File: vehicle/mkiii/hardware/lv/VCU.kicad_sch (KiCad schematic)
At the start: 0 parts

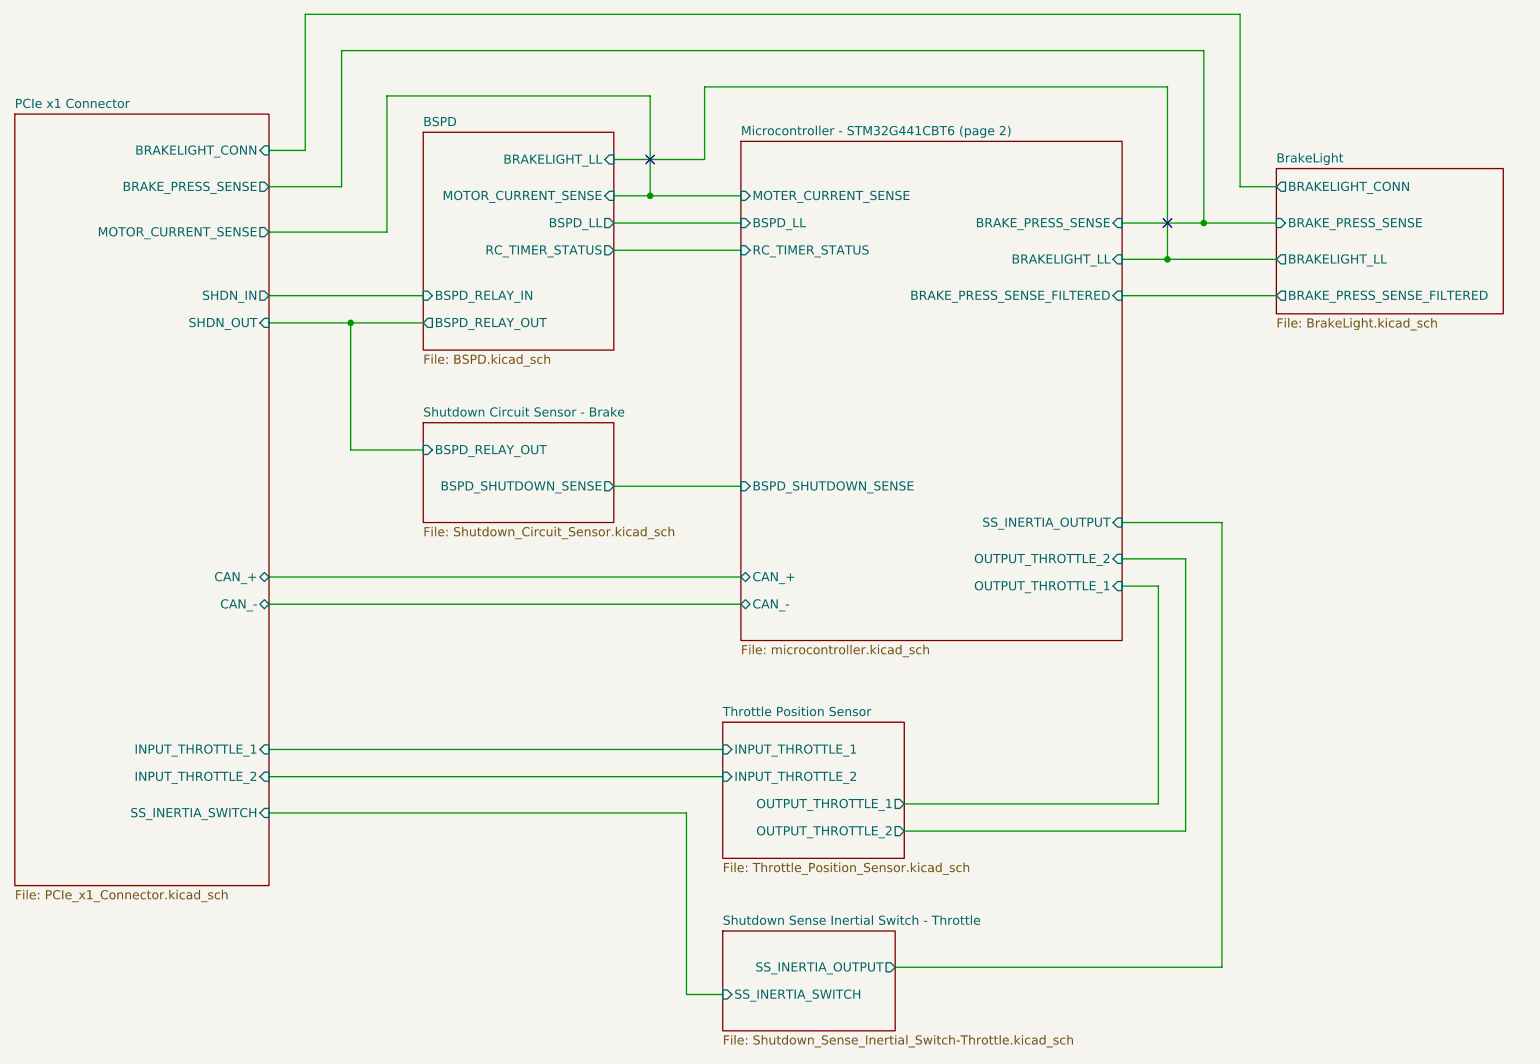
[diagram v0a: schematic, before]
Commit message: Updated title blocks in schematic sheets to include author, set sheet titles, and merged throttle and brake shutdown sense sheets into a single sheet - Shutdown_Sensors.kicad_sch.
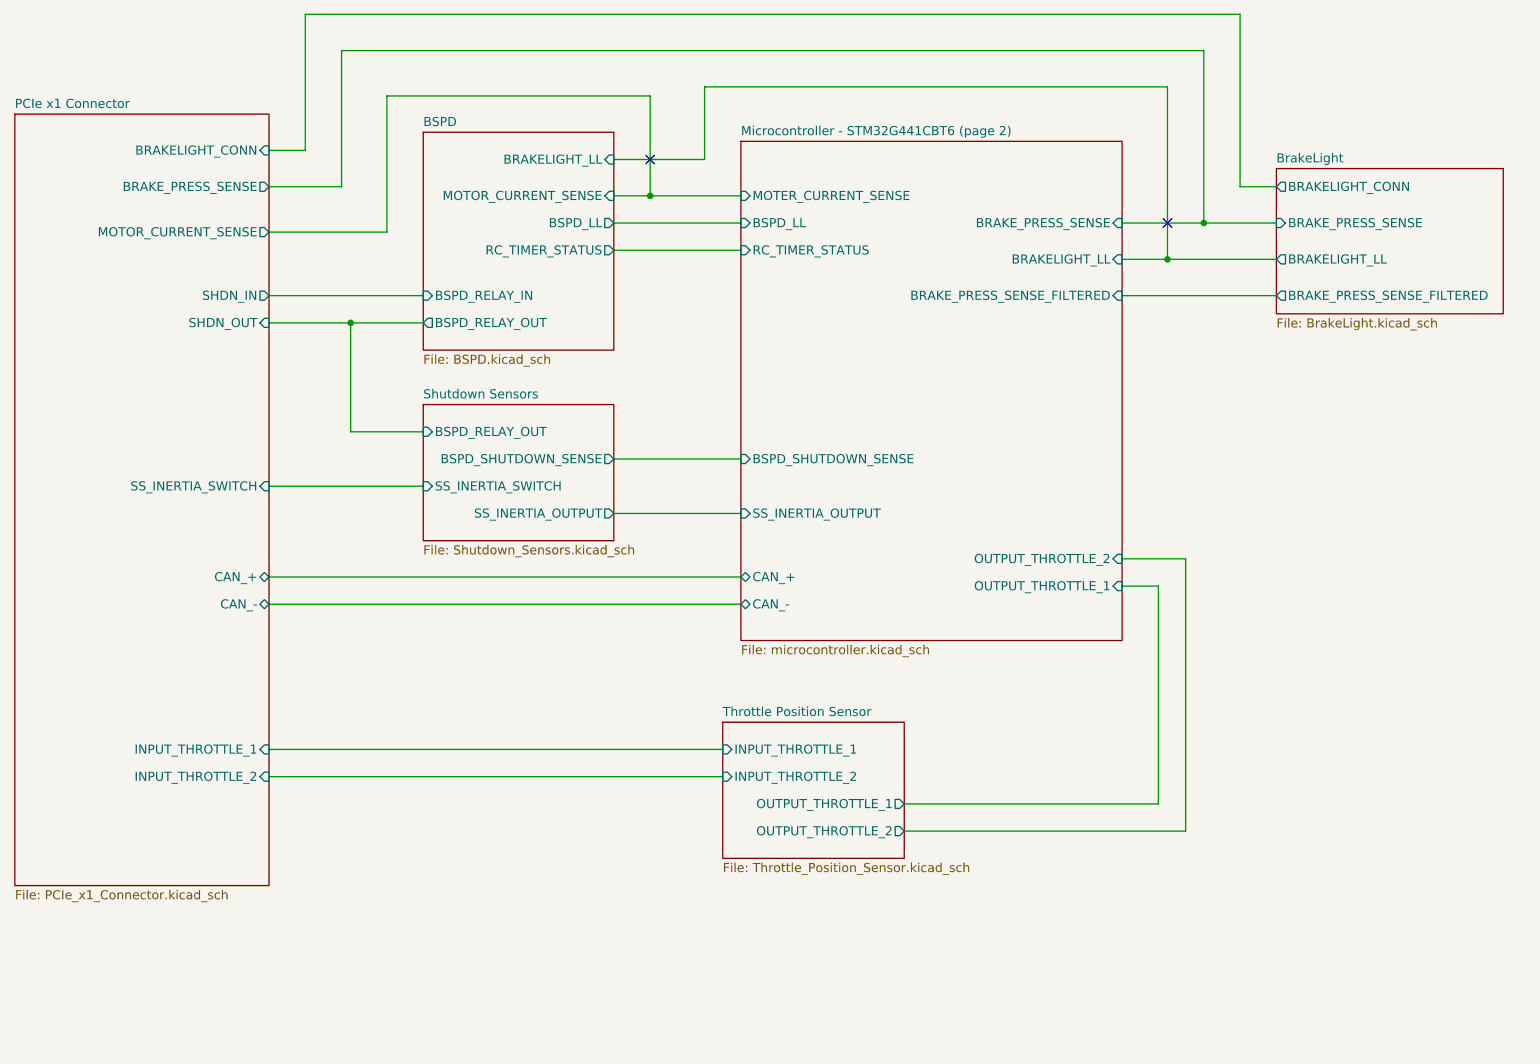
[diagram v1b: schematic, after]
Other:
- sheet Shutdown Sense Inertial Switch - Throttle renamed Shutdown Sensors
- removed sheet Shutdown Circuit Sensor - Brake
- sheet Shutdown Sensors: file Shutdown_Sense_Inertial_Switch-Throttle.kicad_sch -> Shutdown_Sensors.kicad_sch
- sheet Shutdown Sensors ports: added BSPD_RELAY_OUT, BSPD_SHUTDOWN_SENSE; removed none
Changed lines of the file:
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@@
 	(wire
 		(pts
-			(xy 81.28 60.96) (xy 81.28 78.74)
+			(xy 81.28 60.96) (xy 81.28 76.2)
 		)
 		(stroke
@@
 	(wire
 		(pts
+			(xy 118.11 80.01) (xy 135.89 80.01)
+		)
+		(stroke
+			(width 0)
+			(type default)
+		)
+	)
+	(wire
+		(pts
 			(xy 69.85 124.46) (xy 133.35 124.46)
 		)
@@
 	(wire
 		(pts
-			(xy 81.28 78.74) (xy 91.44 78.74)
-		)
-		(stroke
-			(width 0)
-			(type default)
-		)
-	)
-	(wire
-		(pts
 			(xy 69.85 60.96) (xy 81.28 60.96)
 		)
@@
 	(wire
 		(pts
-			(xy 118.11 83.82) (xy 135.89 83.82)
-		)
-		(stroke
-			(width 0)
-			(type default)
-		)
-	)
-	(wire
-		(pts
 			(xy 200.66 22.86) (xy 200.66 46.99)
 		)
@@
 	(wire
 		(pts
-			(xy 69.85 129.54) (xy 128.27 129.54)
-		)
-		(stroke
-			(width 0)
-			(type default)
-		)
-	)
-	(wire
-		(pts
 			(xy 189.23 57.15) (xy 210.82 57.15)
 		)
@@
 	(wire
 		(pts
-			(xy 128.27 154.94) (xy 133.35 154.94)
-		)
-		(stroke
-			(width 0)
-			(type default)
-		)
-	)
-	(wire
-		(pts
 			(xy 130.81 38.1) (xy 130.81 27.94)
 		)
@@
 	(wire
 		(pts
-			(xy 128.27 129.54) (xy 128.27 154.94)
-		)
-		(stroke
-			(width 0)
-			(type default)
-		)
-	)
-	(wire
-		(pts
 			(xy 74.93 17.78) (xy 205.74 17.78)
 		)
@@
 	(wire
 		(pts
+			(xy 118.11 87.63) (xy 135.89 87.63)
+		)
+		(stroke
+			(width 0)
+			(type default)
+		)
+	)
+	(wire
+		(pts
 			(xy 69.85 36.83) (xy 74.93 36.83)
 		)
@@
 	(wire
 		(pts
+			(xy 81.28 76.2) (xy 91.44 76.2)
+		)
+		(stroke
+			(width 0)
+			(type default)
+		)
+	)
+	(wire
+		(pts
 			(xy 81.28 60.96) (xy 91.44 60.96)
 		)
@@
 	(wire
 		(pts
-			(xy 203.2 88.9) (xy 189.23 88.9)
-		)
-		(stroke
-			(width 0)
-			(type default)
-		)
-	)
-	(wire
-		(pts
-			(xy 203.2 151.13) (xy 203.2 88.9)
+			(xy 69.85 83.82) (xy 91.44 83.82)
 		)
 		(stroke
@@
 			(width 0)
 			(type default)
-		)
-	)
-	(wire
-		(pts
-			(xy 157.48 151.13) (xy 203.2 151.13)
-		)
-		(stroke
-			(width 0)
-			(type default)
-		)
-	)
-	(sheet
-		(at 91.44 74.93)
-		(size 26.67 13.97)
-		(exclude_from_sim no)
-		(in_bom yes)
-		(on_board yes)
-		(dnp no)
-		(fields_autoplaced yes)
-		(stroke
-			(width 0.1524)
-			(type solid)
-		)
-		(fill
-			(color 0 0 0 0.0000)
-		)
-		(property "Sheetname" "Shutdown Circuit Sensor - Brake"
-			(at 91.44 74.2184 0)
-			(effects
-				(font
-					(size 1.27 1.27)
-				)
-				(justify left bottom)
-			)
-		)
-		(property "Sheetfile" "Shutdown_Circuit_Sensor.kicad_sch"
-			(at 91.44 89.4846 0)
-			(effects
-				(font
-					(size 1.27 1.27)
-				)
-				(justify left top)
-			)
-		)
-		(pin "BSPD_RELAY_OUT" input
-			(at 91.44 78.74 180)
-			(effects
-				(font
-					(size 1.27 1.27)
-				)
-				(justify left)
-			)
-		)
-		(pin "BSPD_SHUTDOWN_SENSE" output
-			(at 118.11 83.82 0)
-			(effects
-				(font
-					(size 1.27 1.27)
-				)
-				(justify right)
-			)
-		)
-		(instances
-			(project "VCU"
-				(path "/ec5dd9e3-3092-4af4-bee1-94131d9ab7f8"
-					(page "7")
-				)
-			)
 		)
 	)
@@
 		)
 		(pin "SS_INERTIA_SWITCH" input
-			(at 69.85 129.54 0)
+			(at 69.85 83.82 0)
 			(effects
 				(font
@@
 	)
 	(sheet
-		(at 133.35 146.05)
-		(size 24.13 13.97)
+		(at 91.44 72.39)
+		(size 26.67 19.05)
 		(exclude_from_sim no)
 		(in_bom yes)
@@
 			(color 0 0 0 0.0000)
 		)
-		(property "Sheetname" "Shutdown Sense Inertial Switch - Throttle"
-			(at 133.35 145.3384 0)
+		(property "Sheetname" "Shutdown Sensors"
+			(at 91.44 71.6784 0)
 			(effects
 				(font
@@
 			)
 		)
-		(property "Sheetfile" "Shutdown_Sense_Inertial_Switch-Throttle.kicad_sch"
-			(at 133.35 160.6046 0)
+		(property "Sheetfile" "Shutdown_Sensors.kicad_sch"
+			(at 91.44 92.0246 0)
 			(effects
 				(font
@@
 		)
 		(pin "SS_INERTIA_OUTPUT" output
-			(at 157.48 151.13 0)
+			(at 118.11 87.63 0)
 			(effects
 				(font
@@
 		)
 		(pin "SS_INERTIA_SWITCH" input
-			(at 133.35 154.94 180)
-			(effects
-				(font
-					(size 1.27 1.27)
-				)
-				(justify left)
+			(at 91.44 83.82 180)
+			(effects
+				(font
+					(size 1.27 1.27)
+				)
+				(justify left)
+			)
+		)
+		(pin "BSPD_RELAY_OUT" input
+			(at 91.44 76.2 180)
+			(effects
+				(font
+					(size 1.27 1.27)
+				)
+				(justify left)
+			)
+		)
+		(pin "BSPD_SHUTDOWN_SENSE" output
+			(at 118.11 80.01 0)
+			(effects
+				(font
+					(size 1.27 1.27)
+				)
+				(justify right)
 			)
 		)
@@
 		)
 		(pin "BSPD_SHUTDOWN_SENSE" input
-			(at 135.89 83.82 180)
+			(at 135.89 80.01 180)
 			(effects
 				(font
@@
 		)
 		(pin "SS_INERTIA_OUTPUT" input
-			(at 189.23 88.9 0)
-			(effects
-				(font
-					(size 1.27 1.27)
-				)
-				(justify right)
-			)
-		)
+			(at 135.89 87.63 180)
+			(effects
+				(font
+					(size 1.27 1.27)
+				)
+				(justify left)
+			)
+		)
